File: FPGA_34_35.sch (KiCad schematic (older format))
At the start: 1 part, among them U1 XC7A200T-FBG484

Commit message: BOM updated, 25MHz clock level fixed
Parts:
- U1: symbol AMC_FMC_Carrier-PcbDoc-rescue:XC7A200T-FBG484-FPGA_Xilinx_Artix7 -> AMC_FMC_Carrier-PcbDoc-rescue:XC7A200T-FBG484-FPGA_Xilinx_Artix7-AMC_FMC_Carrier-PcbDoc-rescue
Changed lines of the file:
@@
 $EndDescr
 $Comp
-L AMC_FMC_Carrier-PcbDoc-rescue:XC7A200T-FBG484-FPGA_Xilinx_Artix7 U?
+L AMC_FMC_Carrier-PcbDoc-rescue:XC7A200T-FBG484-FPGA_Xilinx_Artix7-AMC_FMC_Carrier-PcbDoc-rescue U?
 U 3 1 5C8DFB5E
 P 8350 4650

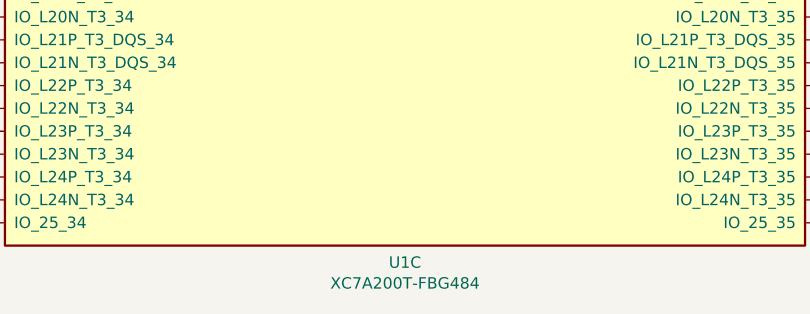
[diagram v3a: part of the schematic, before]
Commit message: BOM configuration file edited, updated Marble picture, some components part number changed
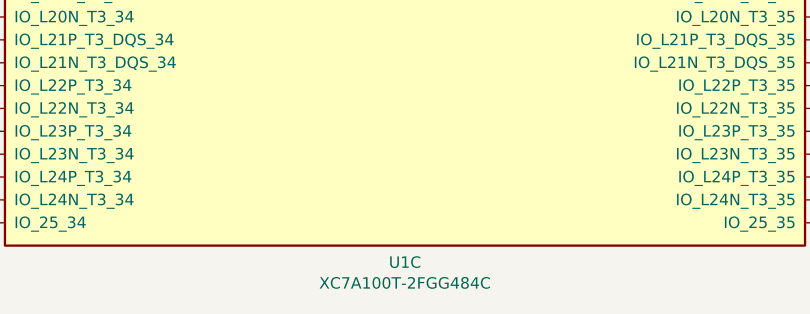
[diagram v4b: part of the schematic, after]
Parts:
- U1: value XC7A200T-FBG484 -> XC7A100T-2FGG484C; Manufacturer Part Number (none) -> XC7A100T-2FGG484C
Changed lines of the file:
@@
 $Descr A3 16535 11693
 encoding utf-8
-Sheet 20 25
+Sheet 19 25
 Title "Marble"
 Date "2019-01-16"
@@
 AR Path="/5C907554/5C721515/5C8DFB5E" Ref="U1"  Part="3"
 F 0 "U1" H 8350 1676 50  0000 C CNN
-F 1 "XC7A200T-FBG484" H 8350 1585 50  0000 C CNN
+F 1 "XC7A100T-2FGG484C" H 8350 1585 50  0000 C CNN
 F 2 "ICs And Semiconductors SMD_BGA:BGA484C100P22X22_2300X2300X240" H 8350 4650 50  0001 C CNN
 F 3 "" H 8350 4650 50  0000 C CNN
+F 4 "XC7A100T-2FGG484C" H 8350 4650 50  0001 C CNN "Manufacturer Part Number"
 	3    8350 4650
 	1    0    0    -1
